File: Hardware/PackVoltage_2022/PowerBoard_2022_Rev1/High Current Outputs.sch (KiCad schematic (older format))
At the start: 20 parts

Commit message: Created global tags in main sheet
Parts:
- U? (x2): symbol MRDT_ICs:LT1910 -> PowerBoard_2022_Rev1-rescue:LT1910-MRDT_ICs
- U? (x2): symbol MRDT_ICs:INA281 -> PowerBoard_2022_Rev1-rescue:INA281-MRDT_ICs
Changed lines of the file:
@@
 $EndDescr
 $Comp
-L MRDT_ICs:LT1910 U?
+L PowerBoard_2022_Rev1-rescue:LT1910-MRDT_ICs U?
 U 1 1 619034E0
 P 1750 2150
@@
 	4150 2600 4150 2700
 $Comp
-L MRDT_ICs:INA281 U?
+L PowerBoard_2022_Rev1-rescue:INA281-MRDT_ICs U?
 U 1 1 61903531
 P 4300 1850
@@
 	2850 1350 2850 1300
 $Comp
-L MRDT_ICs:LT1910 U?
+L PowerBoard_2022_Rev1-rescue:LT1910-MRDT_ICs U?
 U 1 1 6191E0EE
 P 6700 2300
@@
 	9100 2750 9100 2850
 $Comp
-L MRDT_ICs:INA281 U?
+L PowerBoard_2022_Rev1-rescue:INA281-MRDT_ICs U?
 U 1 1 6191E13F
 P 9250 2000

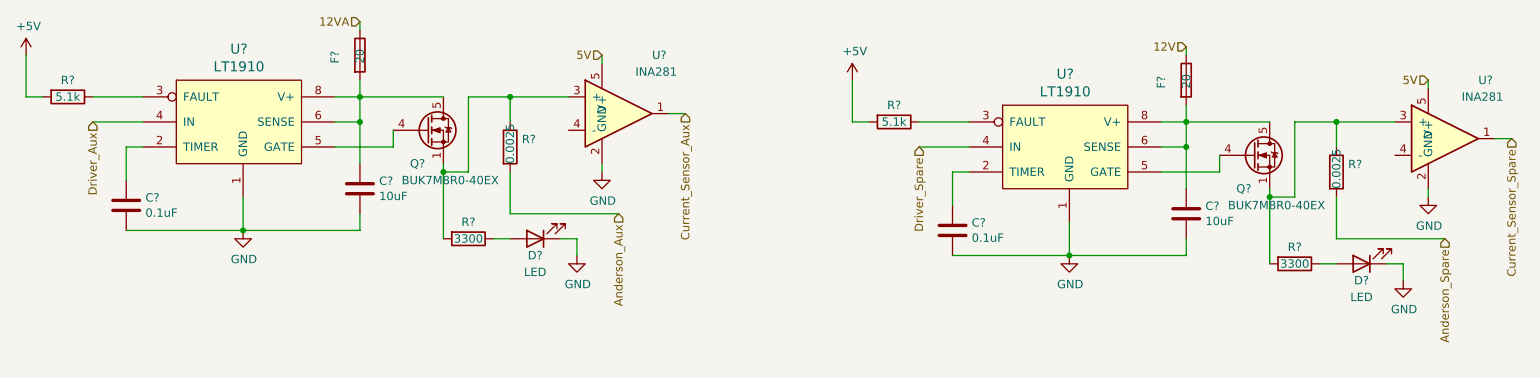
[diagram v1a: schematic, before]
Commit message: TIVA and fixed 12V
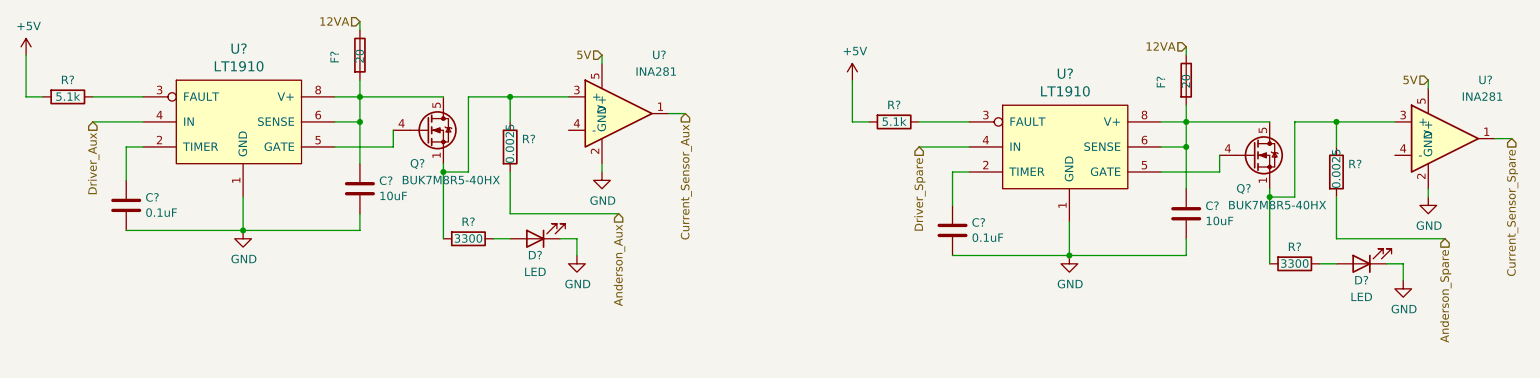
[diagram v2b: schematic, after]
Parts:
- Q? (x2): value BUK7M8R0-40EX -> BUK7M8R5-40HX
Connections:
- net 12V is gone; now on net 12VA: F?.1
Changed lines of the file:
@@
 $Descr A4 11693 8268
 encoding utf-8
-Sheet 8 10
+Sheet 8 9
 Title ""
 Date ""
@@
 AR Path="/615D7BA0/6170B6A9/6190350A" Ref="Q?"  Part="1"
 F 0 "Q?" H 3150 1750 50  0000 L CNN
-F 1 "BUK7M8R0-40EX" H 3100 1650 50  0000 L CNN
+F 1 "BUK7M8R5-40HX" H 3100 1650 50  0000 L CNN
 F 2 "Package_TO_SOT_SMD:LFPAK33" H 3450 1875 50  0001 L CIN
 F 3 "https://assets.nexperia.com/documents/data-sheet/BUK7M8R0-40E.pdf" V 3250 1950 50  0001 L CNN
@@
 AR Path="/615D7BA0/6170B6A9/6191E118" Ref="Q?"  Part="1"
 F 0 "Q?" H 8100 1900 50  0000 L CNN
-F 1 "BUK7M8R0-40EX" H 8050 1800 50  0000 L CNN
+F 1 "BUK7M8R5-40HX" H 8050 1800 50  0000 L CNN
 F 2 "Package_TO_SOT_SMD:LFPAK33" H 8400 2025 50  0001 L CIN
 F 3 "https://assets.nexperia.com/documents/data-sheet/BUK7M8R0-40E.pdf" V 8200 2100 50  0001 L CNN
@@
 	9250 1650 9250 1700
 Text HLabel 7800 1450 0    50   Input ~ 0
-12V
+12VA
 Wire Wire Line
 	7800 1500 7800 1450

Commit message: Fixed some stuff
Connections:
- net Anderson_Aux: now also U?.4 (-)
- net Anderson_Spare: now also U?.4 (-)
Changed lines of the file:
@@
 $Descr A4 11693 8268
 encoding utf-8
-Sheet 8 9
+Sheet 7 9
 Title ""
 Date ""
@@
 	3750 2450 4400 2450
 Wire Wire Line
-	3750 2200 3750 2450
+	3750 2200 3750 2300
 Wire Wire Line
 	3350 2150 3350 2200
@@
 	8700 2600 9350 2600
 Wire Wire Line
-	8700 2350 8700 2600
+	8700 2350 8700 2450
 Wire Wire Line
 	8300 2300 8300 2350
@@
 Wire Wire Line
 	7800 1500 7800 1450
+Wire Wire Line
+	4100 1950 4100 2300
+Wire Wire Line
+	4100 2300 3750 2300
+Connection ~ 3750 2300
+Wire Wire Line
+	3750 2300 3750 2450
+Wire Wire Line
+	9050 2100 9050 2450
+Wire Wire Line
+	9050 2450 8700 2450
+Connection ~ 8700 2450
+Wire Wire Line
+	8700 2450 8700 2600
 $EndSCHEMATC

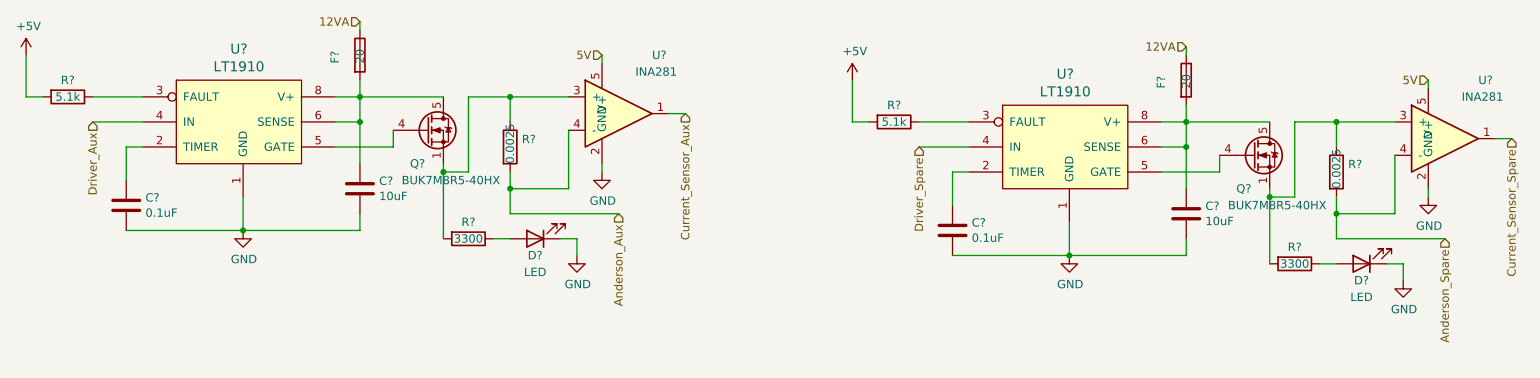
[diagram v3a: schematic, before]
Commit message: Changed values of LED resistors, changed some of the outputs to inputs, and made board look better
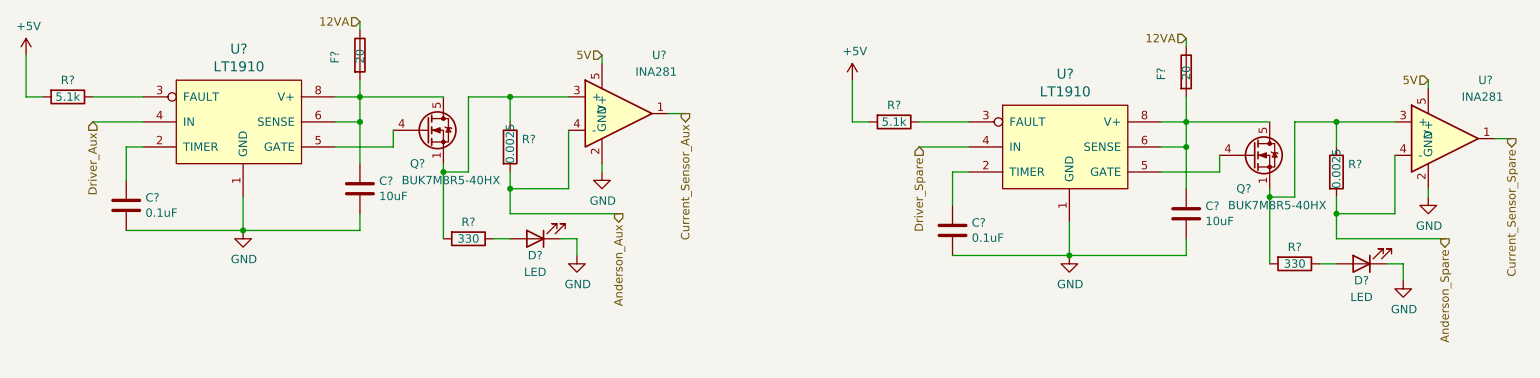
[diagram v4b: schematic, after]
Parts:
- removed F?: 20, symbol Device:Fuse
- added F?: 20, symbol Device:Fuse
- R? (x2): value 3300 -> 330
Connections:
- net 12VA: now also F?.1
- net at C?.1, Q?.5 (D), U?.6 (SENSE)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: now also F?.2
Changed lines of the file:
@@
 $Descr A4 11693 8268
 encoding utf-8
-Sheet 7 9
+Sheet 6 9
 Title ""
 Date ""
@@
 AR Path="/615D7BA0/6170B6A9/6190351D" Ref="R?"  Part="1"
 F 0 "R?" V 3400 2600 50  0000 C CNN
-F 1 "3300" V 3500 2600 50  0000 C CNN
+F 1 "330" V 3500 2600 50  0000 C CNN
 F 2 "" V 3430 2600 50  0001 C CNN
 F 3 "~" H 3500 2600 50  0001 C CNN
@@
 Wire Wire Line
 	1550 1900 1250 1900
-Text HLabel 4400 2450 3    50   Input ~ 0
+Text HLabel 4400 2450 3    50   Output ~ 0
 Anderson_Aux
 Text HLabel 1250 1900 3    50   Input ~ 0
 Driver_Aux
-Text HLabel 4800 1850 3    50   Input ~ 0
+Text HLabel 4800 1850 3    50   Output ~ 0
 Current_Sensor_Aux
 Wire Wire Line
@@
 	1    0    0    -1
 $EndComp
-$Comp
-L Device:Fuse F?
-U 1 1 6191E111
-P 7800 1650
-AR Path="/615D5992/6191E111" Ref="F?"  Part="1"
-AR Path="/615D7BA0/6170B60A/6191E111" Ref="F?"  Part="1"
-AR Path="/615D7BA0/6170B6A9/6191E111" Ref="F?"  Part="1"
-F 0 "F?" V 7650 1600 50  0000 L CNN
-F 1 "20" V 7800 1600 50  0000 L CNN
-F 2 "" V 7730 1650 50  0001 C CNN
-F 3 "~" H 7800 1650 50  0001 C CNN
-	1    7800 1650
-	1    0    0    -1
-$EndComp
 Wire Wire Line
 	7650 1900 7800 1900
@@
 Wire Wire Line
 	7800 1900 8300 1900
-Wire Wire Line
-	7800 1800 7800 1900
 Connection ~ 7800 1900
 Wire Wire Line
@@
 AR Path="/615D7BA0/6170B6A9/6191E12B" Ref="R?"  Part="1"
 F 0 "R?" V 8350 2750 50  0000 C CNN
-F 1 "3300" V 8450 2750 50  0000 C CNN
+F 1 "330" V 8450 2750 50  0000 C CNN
 F 2 "" V 8380 2750 50  0001 C CNN
 F 3 "~" H 8450 2750 50  0001 C CNN
@@
 Wire Wire Line
 	6500 2050 6200 2050
-Text HLabel 9350 2600 3    50   Input ~ 0
+Text HLabel 9350 2600 3    50   Output ~ 0
 Anderson_Spare
 Text HLabel 6200 2050 3    50   Input ~ 0
 Driver_Spare
-Text HLabel 9750 2000 3    50   Input ~ 0
+Text HLabel 9750 2000 3    50   Output ~ 0
 Current_Sensor_Spare
 Wire Wire Line
@@
 Wire Wire Line
 	9250 1650 9250 1700
-Text HLabel 7800 1450 0    50   Input ~ 0
-12VA
-Wire Wire Line
-	7800 1500 7800 1450
 Wire Wire Line
 	4100 1950 4100 2300
@@
 Wire Wire Line
 	8700 2450 8700 2600
+$Comp
+L Device:Fuse F?
+U 1 1 6185444D
+P 7800 1600
+AR Path="/615D5992/6185444D" Ref="F?"  Part="1"
+AR Path="/615D7BA0/6170B60A/6185444D" Ref="F?"  Part="1"
+AR Path="/615D7BA0/6170B6A9/6185444D" Ref="F?"  Part="1"
+F 0 "F?" V 7650 1550 50  0000 L CNN
+F 1 "20" V 7800 1550 50  0000 L CNN
+F 2 "" V 7730 1600 50  0001 C CNN
+F 3 "~" H 7800 1600 50  0001 C CNN
+	1    7800 1600
+	1    0    0    -1
+$EndComp
+Text HLabel 7800 1400 0    50   Input ~ 0
+12VA
+Wire Wire Line
+	7800 1450 7800 1400
+Wire Wire Line
+	7800 1750 7800 1900
 $EndSCHEMATC

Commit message: Minor changes with Powerboard PDF
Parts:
- gave numbers to parts that had none: 20
